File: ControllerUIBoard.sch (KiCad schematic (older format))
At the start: 20 parts, among them J10 ATMEGA_ICSP, U4 ATmega2560-16AU, Y2 16MHz

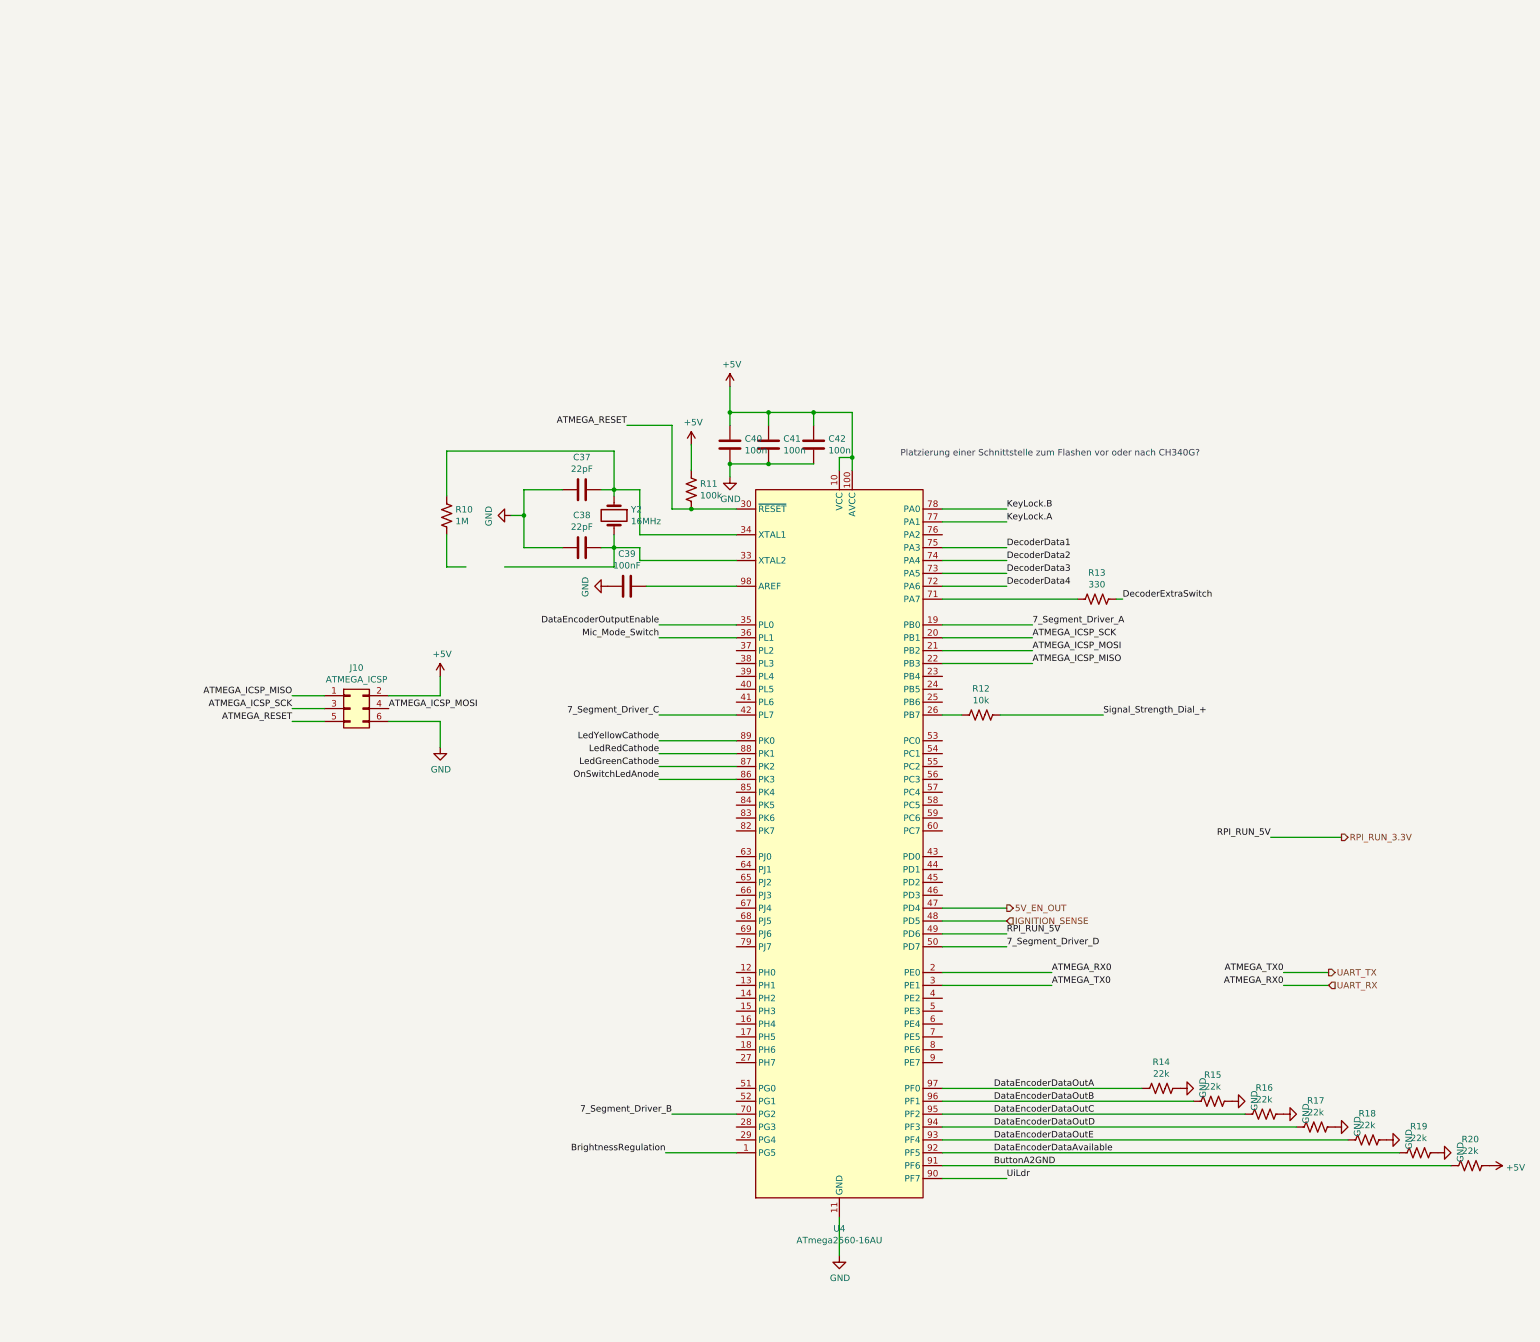
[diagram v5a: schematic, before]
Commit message: [added:] ATMEGA 4809 integration
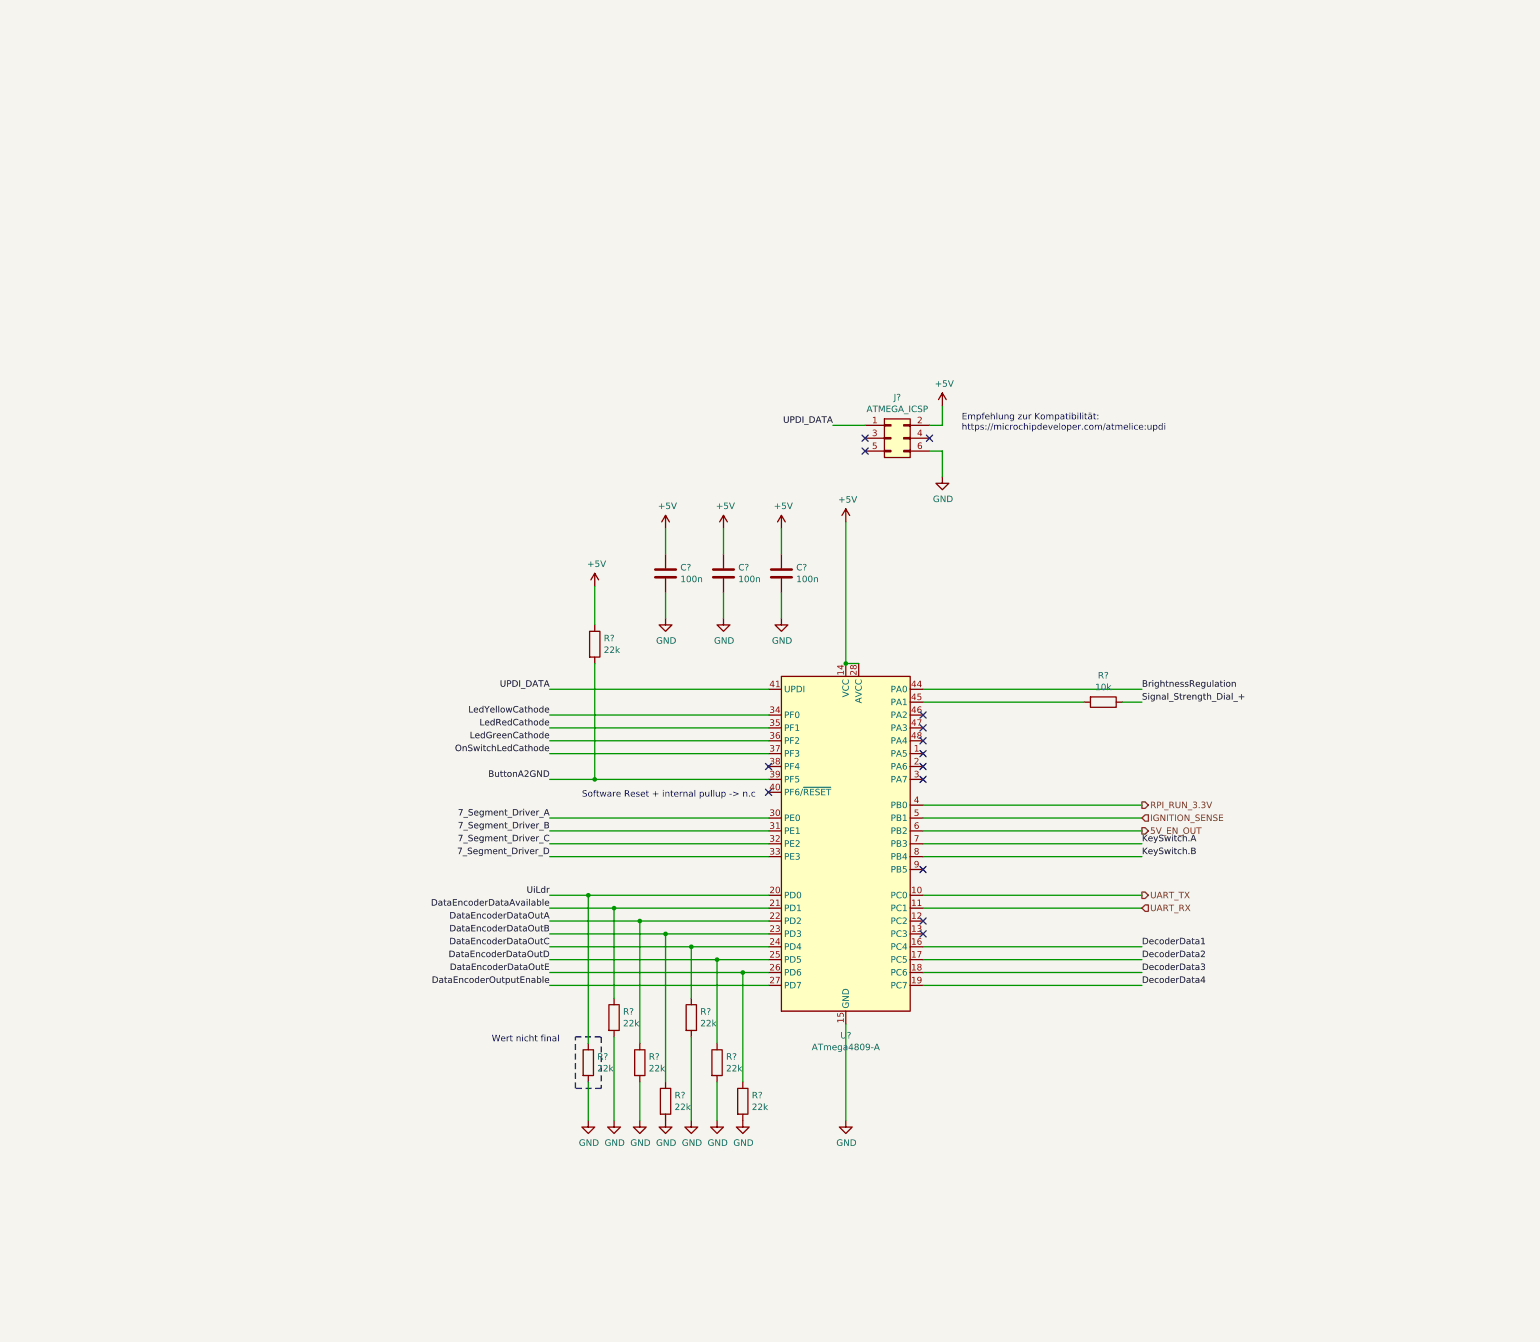
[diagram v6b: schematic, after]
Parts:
- removed C37, C38: 22pF, Capacitor_SMD:C_0603_1608Metric, symbol Device:C
- removed C39: 100nF, Capacitor_SMD:C_0603_1608Metric, symbol Device:C
- removed C41, C42: 100n, Capacitor_SMD:C_0603_1608Metric, symbol Device:C
- removed R10: 1M, Resistor_SMD:R_0402_1005Metric, symbol Device:R_US
- removed R11: 100k, Resistor_SMD:R_0402_1005Metric, symbol Device:R_US
- removed R12: 10k, Resistor_SMD:R_0402_1005Metric, symbol Device:R_US
- removed R13: 330, symbol Device:R_US
- removed R14, R15, R16, R17, R18, R19, R20: 22k, Resistor_SMD:R_0402_1005Metric, symbol Device:R_US
- removed U4: ATmega2560-16AU, Package_QFP:TQFP-100_14x14mm_P0.5mm, symbol MCU_Microchip_ATmega:ATmega2560-16AU
- removed Y2: 16MHz, Crystal:Crystal_SMD_Abracon_ABM3-2Pin_5.0x3.2mm, symbol Device:Crystal
- added C? (x2): 100n, Capacitor_SMD:C_0603_1608Metric, symbol Device:C
- added R? (x8): 22k, symbol Device:R
- added R?: 10k, symbol Device:R
- added U?: ATmega4809-A, Package_QFP:TQFP-48_7x7mm_P0.5mm, symbol MCU_Microchip_ATmega:ATmega4809-A
- renumbered C40 to C?, J10 to J?
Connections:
- net +5V: now also C?.1, C?.1, R?.1, U?.14 (VCC), U?.28 (AVCC), U?.42 (VCC)
- net 5V_EN_OUT: now also U?.6 (PB2)
- net 7_Segment_Driver_A: now also U?.30 (PE0)
- net 7_Segment_Driver_B: now also U?.31 (PE1)
- net 7_Segment_Driver_C: now also U?.32 (PE2)
- net 7_Segment_Driver_D: now also U?.33 (PE3)
- net BrightnessRegulation: now also U?.44 (PA0)
- net ButtonA2GND: now also R?.2, U?.39 (PF5)
- net DataEncoderDataAvailable: now also R?.1, U?.21 (PD1)
- net DataEncoderDataOutA: now also R?.1, U?.22 (PD2)
- net DataEncoderDataOutB: now also R?.1, U?.23 (PD3)
- net DataEncoderDataOutC: now also R?.1, U?.24 (PD4)
- net DataEncoderDataOutD: now also R?.1, U?.25 (PD5)
- net DataEncoderDataOutE: now also R?.1, U?.26 (PD6)
- net DataEncoderOutputEnable: now also U?.27 (PD7)
- net DecoderData1: now also U?.16 (PC4)
- net DecoderData2: now also U?.17 (PC5)
- net DecoderData3: now also U?.18 (PC6)
- net DecoderData4: now also U?.19 (PC7)
- net GND: now also C?.2, C?.2, R?.2, R?.2, R?.2, R?.2, R?.2, R?.2, R?.2, U?.15 (GND), U?.29 (GND), U?.43 (GND)
- net IGNITION_SENSE: now also U?.5 (PB1)
- net LedGreenCathode: now also U?.36 (PF2)
- net LedRedCathode: now also U?.35 (PF1)
- net LedYellowCathode: now also U?.34 (PF0)
- net RPI_RUN_3.3V: now also U?.4 (PB0)
- net Signal_Strength_Dial_+: now also R?.1
- net UART_RX: now also U?.11 (PC1)
- net UART_TX: now also U?.10 (PC0)
- net UiLdr: now also R?.1, U?.20 (PD0)
- net ATMEGA_ICSP_MISO renamed UPDI_DATA
- net UPDI_DATA: now also U?.41 (UPDI)
- net ATMEGA_ICSP_MOSI: no longer names the net of J?.4 (Pin_4)
- net ATMEGA_ICSP_SCK: no longer names the net of J?.3 (Pin_3)
- net ATMEGA_RESET: no longer names the net of J?.5 (Pin_5)
- new net: R?.2, U?.45 (PA1)
- new net KeySwitch.A: U?.7 (PB3)
- new net KeySwitch.B: U?.8 (PB4)
- new net OnSwitchLedCathode: U?.37 (PF3)
- no-connect marks 0 -> 14
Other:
- note added: "Empfehlung zur Kompatibilität:\nhttps://microchipdeveloper.com/atmelice:updi"
- note added: "Software Reset + internal pullup -> n.c"
- note added: "Wert nicht final"
- note removed: "Platzierung einer Schnittstelle zum Flashen vor oder nach CH340G?"
- moved on the sheet: C?, J?

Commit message: - Zwischenstand Display Driving
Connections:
- net 7_Segment_Driver_A renamed 7Seg_Driver_A
- net 7_Segment_Driver_B renamed 7Seg_Driver_B
- net 7_Segment_Driver_C renamed 7Seg_Driver_C
- net 7_Segment_Driver_D renamed 7Seg_Driver_D
- net DecoderData1 renamed 7Seg_Decoder_D1
- net DecoderData2 renamed 7Seg_Decoder_D2
- net DecoderData3 renamed 7Seg_Decoder_D3
- net DecoderData4 renamed 7Seg_Decoder_D4
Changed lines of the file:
@@
 Text HLabel 8300 4200 2    50   Output ~ 0
 5V_EN_OUT
-Text Label 8300 5400 0    50   ~ 0
-DecoderData4
-Text Label 8300 5300 0    50   ~ 0
-DecoderData3
-Text Label 8300 5200 0    50   ~ 0
-DecoderData2
-Text Label 8300 5100 0    50   ~ 0
-DecoderData1
 Text Label 3700 3600 2    50   ~ 0
 OnSwitchLedCathode
@@
 Wire Wire Line
 	6600 4700 8300 4700
-Text Label 3700 4100 2    50   ~ 0
-7_Segment_Driver_A
-Text Label 3700 4200 2    50   ~ 0
-7_Segment_Driver_B
-Text Label 3700 4300 2    50   ~ 0
-7_Segment_Driver_C
-Text Label 3700 4400 2    50   ~ 0
-7_Segment_Driver_D
 Text Label 8300 4300 0    50   ~ 0
 KeySwitch.A
@@
 Wire Wire Line
 	8150 3200 8300 3200
-Text Label 8300 3100 0    50   ~ 0
-BrightnessRegulation
 Wire Wire Line
 	6600 3100 8300 3100
@@
 Text Notes 6900 1100 0    50   ~ 0
 Empfehlung zur Kompatibilität:\nhttps://microchipdeveloper.com/atmelice:updi
+Text HLabel 3700 4400 0    50   Output ~ 0
+7Seg_Driver_D
+Text HLabel 3700 4300 0    50   Output ~ 0
+7Seg_Driver_C
+Text HLabel 3700 4200 0    50   Output ~ 0
+7Seg_Driver_B
+Text HLabel 3700 4100 0    50   Output ~ 0
+7Seg_Driver_A
+Text HLabel 8300 5300 2    50   Output ~ 0
+7Seg_Decoder_D3
+Text HLabel 8300 5400 2    50   Output ~ 0
+7Seg_Decoder_D4
+Text HLabel 8300 5200 2    50   Output ~ 0
+7Seg_Decoder_D2
+Text HLabel 8300 5100 2    50   Output ~ 0
+7Seg_Decoder_D1
+Text HLabel 8300 3100 2    50   Output ~ 0
+BrightnessRegulation
 $EndSCHEMATC

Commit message: Umsortiert
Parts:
- added J?: Conn_02x08_Odd_Even, Connector_PinSocket_2.54mm:PinSocket_2x08_P2.54mm_Vertical, symbol Connector_Generic:Conn_02x08_Odd_Even
- added J?: Conn_02x01, Connector_PinHeader_2.54mm:PinHeader_1x02_P2.54mm_Vertical, symbol Connector_Generic:Conn_02x01
- added J?: Conn_01x03_Male, Connector_PinHeader_2.54mm:PinHeader_1x03_P2.54mm_Vertical, symbol Connector:Conn_01x03_Male
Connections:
- net +5V: now also J?.12 (Pin_12)
- net ButtonA2GND: now also J?.6 (Pin_6)
- net DataEncoderDataAvailable: now also J?.7 (Pin_7)
- net DataEncoderDataOutA: now also J?.11 (Pin_11)
- net DataEncoderDataOutB: now also J?.10 (Pin_10)
- net DataEncoderDataOutC: now also J?.9 (Pin_9)
- net DataEncoderDataOutD: now also J?.16 (Pin_16)
- net DataEncoderDataOutE: now also J?.15 (Pin_15)
- net DataEncoderOutputEnable: now also J?.8 (Pin_8)
- net GND: now also J?.1 (Pin_1), J?.13 (Pin_13), J?.3 (Pin_3)
- net LedGreenCathode: now also J?.3 (Pin_3)
- net LedRedCathode: now also J?.4 (Pin_4)
- net LedYellowCathode: now also J?.2 (Pin_2)
- net Signal_Strength_Dial_+: now also J?.2 (Pin_2)
- net UiLdr: now also J?.1 (Pin_1)
- net BrightnessRegulation renamed BrightnessPWM
- new net KeyLock.A: J?.1 (Pin_1)
- new net KeyLock.B: J?.2 (Pin_2)
- new net OnSwitchLedAnode: J?.14 (Pin_14)
- no-connect marks 14 -> 15
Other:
- note added: "PWM Output\n"
- note added: "Spiegelung um Längsachse nätig, je nach Orientierung"
- note added: "UIBoard interfacing\n"
- moved on the sheet: C?, J?, R?, U?
